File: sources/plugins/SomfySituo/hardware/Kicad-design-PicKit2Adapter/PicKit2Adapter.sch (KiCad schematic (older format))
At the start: 2 parts, among them J1 AVX 00-9188 006, P1 ICSP_PicKit2

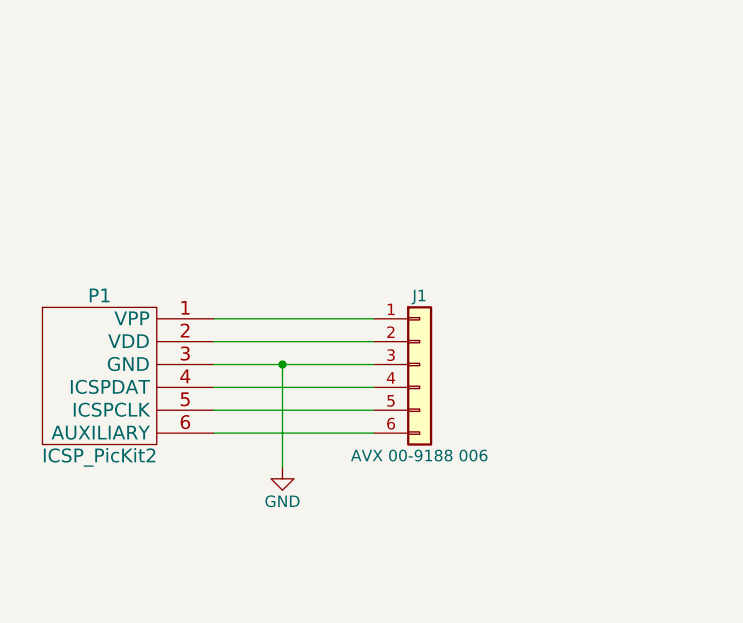
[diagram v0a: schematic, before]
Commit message: Add 4-pins and 8-pins connectors on ICSP adapter
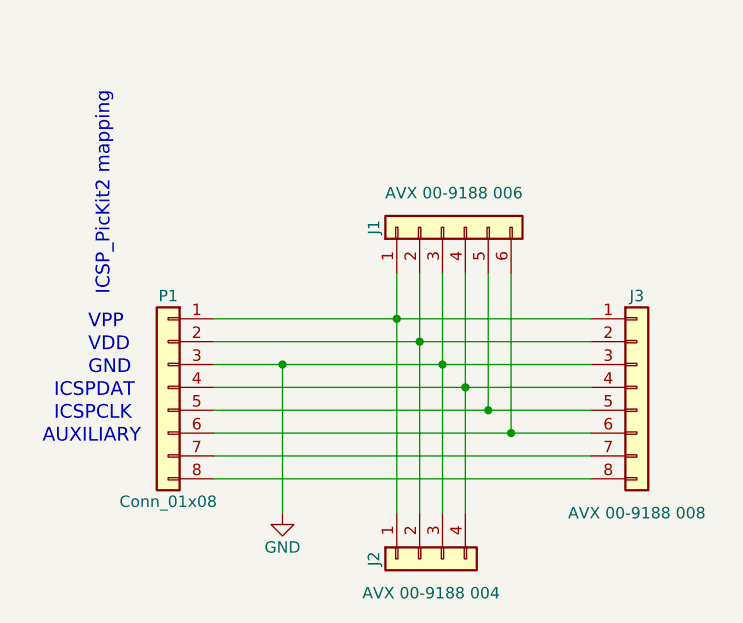
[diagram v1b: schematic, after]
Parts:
- removed P1: ICSP_PicKit2, Pin_Headers:Pin_Header_Angled_1x06_Pitch2.54mm, symbol ICSP_PicKit2
- added J2: AVX 00-9188 004, AVX 00-9188 006:AVX_00-9188_004, symbol Conn_01x04
- added J3: AVX 00-9188 008, AVX 00-9188 006:AVX_00-9188_008, symbol Conn_01x08
- added P1: Conn_01x08, Pin_Headers:Pin_Header_Angled_1x08_Pitch2.54mm, symbol Conn_01x08
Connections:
- net GND: now also J2.3 (Pin_3), J3.3 (Pin_3), P1.3 (Pin_3)
- net at J1.1 (Pin_1): now also J2.1 (Pin_1), J3.1 (Pin_1), P1.1 (Pin_1)
- net at J1.2 (Pin_2): now also J2.2 (Pin_2), J3.2 (Pin_2), P1.2 (Pin_2)
- net at J1.4 (Pin_4): now also J2.4 (Pin_4), J3.4 (Pin_4), P1.4 (Pin_4)
- net at J1.5 (Pin_5): now also J3.5 (Pin_5), P1.5 (Pin_5)
- net at J1.6 (Pin_6): now also J3.6 (Pin_6), P1.6 (Pin_6)
- new net: J3.7 (Pin_7), P1.7 (Pin_7)
- new net: J3.8 (Pin_8), P1.8 (Pin_8)
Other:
- note added: "AUXILIARY"
- note added: "GND"
- note added: "ICSPCLK"
- note added: "ICSPDAT"
- note added: "ICSP_PicKit2 mapping"
- note added: "VDD"
- note added: "VPP"
- moved on the sheet: J1
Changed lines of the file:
@@
 $EndDescr
 $Comp
-L ICSP_PicKit2 P1
-U 1 1 5ABB75B3
-P 3000 2050
-F 0 "P1" H 2850 2400 60  0000 C CNN
-F 1 "ICSP_PicKit2" H 2850 1700 60  0000 C CNN
-F 2 "Pin_Headers:Pin_Header_Angled_1x06_Pitch2.54mm" H 3000 2050 60  0001 C CNN
-F 3 "" H 3000 2050 60  0001 C CNN
-	1    3000 2050
+L Conn_01x06 J1
+U 1 1 5ABB7664
+P 4350 1400
+F 0 "J1" H 4350 1700 50  0000 C CNN
+F 1 "AVX 00-9188 006" V 4500 1350 50  0000 C CNN
+F 2 "AVX 00-9188 006:AVX_00-9188_006" H 4350 1400 50  0001 C CNN
+F 3 "" H 4350 1400 50  0001 C CNN
+	1    4350 1400
+	0    -1   -1   0
+$EndComp
+Wire Wire Line
+	3350 1800 5000 1800
+Wire Wire Line
+	3350 1900 5000 1900
+Wire Wire Line
+	3350 2000 5000 2000
+Wire Wire Line
+	3350 2100 5000 2100
+Wire Wire Line
+	3350 2200 5000 2200
+Wire Wire Line
+	3350 2300 5000 2300
+$Comp
+L GND #PWR1
+U 1 1 5ABB76A8
+P 3650 2650
+F 0 "#PWR1" H 3650 2400 50  0001 C CNN
+F 1 "GND" H 3650 2500 50  0000 C CNN
+F 2 "" H 3650 2650 50  0001 C CNN
+F 3 "" H 3650 2650 50  0001 C CNN
+	1    3650 2650
+	1    0    0    -1
+$EndComp
+Wire Wire Line
+	3650 2000 3650 2650
+Connection ~ 3650 2000
+$Comp
+L Conn_01x08 J3
+U 1 1 5AEC404D
+P 5200 2100
+F 0 "J3" H 5200 2500 50  0000 C CNN
+F 1 "AVX 00-9188 008" H 5200 1550 50  0000 C CNN
+F 2 "AVX 00-9188 006:AVX_00-9188_008" H 5200 2100 50  0001 C CNN
+F 3 "" H 5200 2100 50  0001 C CNN
+	1    5200 2100
 	1    0    0    -1
 $EndComp
 $Comp
-L Conn_01x06 J1
-U 1 1 5ABB7664
-P 4250 2000
-F 0 "J1" H 4250 2300 50  0000 C CNN
-F 1 "AVX 00-9188 006" H 4250 1600 50  0000 C CNN
-F 2 "AVX 00-9188 006:AVX_00-9188_006" H 4250 2000 50  0001 C CNN
-F 3 "" H 4250 2000 50  0001 C CNN
-	1    4250 2000
-	1    0    0    -1
+L Conn_01x04 J2
+U 1 1 5AEC4080
+P 4250 2850
+F 0 "J2" H 4250 3050 50  0000 C CNN
+F 1 "AVX 00-9188 004" V 4400 2800 50  0000 C CNN
+F 2 "AVX 00-9188 006:AVX_00-9188_004" H 4250 2850 50  0001 C CNN
+F 3 "" H 4250 2850 50  0001 C CNN
+	1    4250 2850
+	0    -1   1    0
 $EndComp
+$Comp
+L Conn_01x08 P1
+U 1 1 5AEC40EF
+P 3150 2100
+F 0 "P1" H 3150 2500 50  0000 C CNN
+F 1 "Conn_01x08" H 3150 1600 50  0000 C CNN
+F 2 "Pin_Headers:Pin_Header_Angled_1x08_Pitch2.54mm" H 3150 2100 50  0001 C CNN
+F 3 "" H 3150 2100 50  0001 C CNN
+	1    3150 2100
+	-1   0    0    -1
+$EndComp
+Text Notes 2900 1700 1    60   ~ 0
+ICSP_PicKit2 mapping
+Text Notes 2800 1850 0    60   ~ 0
+VPP
+Text Notes 2800 2050 0    60   ~ 0
+GND
+Text Notes 2650 2150 0    60   ~ 0
+ICSPDAT
+Text Notes 2650 2250 0    60   ~ 0
+ICSPCLK
+Text Notes 2600 2350 0    60   ~ 0
+AUXILIARY
+Text Notes 2800 1950 0    60   ~ 0
+VDD
 Wire Wire Line
-	3350 1800 4050 1800
+	4150 2650 4150 1600
 Wire Wire Line
-	3350 1900 4050 1900
+	4250 1600 4250 2650
 Wire Wire Line
-	3350 2000 4050 2000
+	4350 2650 4350 1600
 Wire Wire Line
-	4050 2100 3350 2100
+	4450 2650 4450 1600
 Wire Wire Line
-	3350 2200 4050 2200
+	4550 2200 4550 1600
 Wire Wire Line
-	4050 2300 3350 2300
-$Comp
-L GND #PWR01
-U 1 1 5ABB76A8
-P 3650 2450
-F 0 "#PWR01" H 3650 2200 50  0001 C CNN
-F 1 "GND" H 3650 2300 50  0000 C CNN
-F 2 "" H 3650 2450 50  0001 C CNN
-F 3 "" H 3650 2450 50  0001 C CNN
-	1    3650 2450
-	1    0    0    -1
-$EndComp
+	4650 2300 4650 1600
+Connection ~ 4450 2100
+Connection ~ 4550 2200
+Connection ~ 4650 2300
 Wire Wire Line
-	3650 2450 3650 2000
-Connection ~ 3650 2000
+	3350 2400 5000 2400
+Wire Wire Line
+	5000 2500 3350 2500
+Connection ~ 4350 2000
+Connection ~ 4250 1900
+Connection ~ 4150 1800
 $EndSCHEMATC
